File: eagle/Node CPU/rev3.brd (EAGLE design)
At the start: 50 x 50 mm, 44 parts, among them IC1 MEGA8-AI

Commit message: updated to revision 3 of the board
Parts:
- removed PC0, PD0: (no value), pinhead:1X01
- removed PWR: (no value), SparkFun-Passives:1X02
- removed X1: (no value), con-wago-500:W237-102
- added C5: 22pF, resistor:C0603
- added GND_1, PC8, PD8: (no value), pinhead:1X01
- added JP1: (no value), SparkFun-Connectors:SCREWTERMINAL-3.5MM-2
- added VCC_1: VCC, pinhead:1X01
- C1: value 0.1uF -> 22pF
- C2: value 22pF -> 0.1uF
- IC1: value MEGA8-AI -> MEGA88
- MCP1: value (none) -> MCP2515
- MCP2: value MCP2551DIL8 -> MCP2551
- moved PC4 43.1 mm to (32.8, 47.8)
- moved PC7 38.1 mm to (2.29, 17.3)
- moved PC6 38.1 mm to (2.29, 24.9)
- moved PD1 38.1 mm to (48.0, 24.9)
- moved PC3 32.3 mm to (25.1, 47.8)
- moved PD5 31.4 mm to (17.5, 2.03)
- moved PD4 30.5 mm to (9.91, 2.03)
- moved PC5 30.5 mm to (2.29, 40.1)
- moved PD2 27.5 mm to (48.0, 17.3)
- moved PD6 27.5 mm to (25.1, 2.03)
- moved PD7 27.5 mm to (32.8, 2.03)
- moved R5 24.7 mm to (10.6, 24.6), turned to 180 degrees
- moved C1 18.0 mm to (17.8, 38.1), turned to 90 degrees
- moved PC2 17.0 mm to (17.5, 47.8)
- moved PD3 17.0 mm to (48.0, 9.65)
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- renumbered MCP2551 to MCP2
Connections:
- removed net N$36: MCP2.6, X1.2
- new net N$38: MCP1.15, MISO.1, R3.2
- new net N$39: IC1.17, ISP.4, R2.1
- net GND: now also C3.2, C5.1, GND_1.1; no longer C3.1, PWR.2
- net N$1: now also C1.1, IC1.20; no longer IC1.17, MCP1.13, R2.1, SCK.1
- net N$10: now also JP1.1, MCP2.6; no longer C3.2, IC1.7, XTAL.2
- net N$15: now also MCP1.13, R2.2, SCK.1; no longer ISP.2, R4.2
- net N$16: now also JP1.2, MCP2.7; no longer ISP.3, R3.2
- net N$17: now also IC1.15, ISP.2, R4.1; no longer ISP.4, R2.2
- net N$2: now also ISP.3; no longer MCP1.15, MISO.1
- net N$20: now also PC2.1; no longer PC0.1
- net N$22: now also PC5.1; no longer PC2.1
- net N$23: now also PC6.1; no longer PC3.1
- net N$24: now also PC7.1; no longer PC4.1
- net N$25: now also PC8.1; no longer PC5.1
- net N$26: now also PC4.1; no longer PC6.1
- net N$27: now also PC3.1; no longer PC7.1
- net N$28: now also PD4.1; no longer PD0.1
- net N$29: now also PD5.1; no longer PD1.1
- net N$3: now also R4.2; no longer IC1.15, R4.1
- net N$30: now also PD6.1; no longer PD2.1
- net N$31: now also PD7.1; no longer PD3.1
- net N$32: now also PD8.1; no longer PD4.1
- net N$33: now also PD3.1; no longer PD5.1
- net N$34: now also PD2.1; no longer PD6.1
- net N$35: now also PD1.1; no longer PD7.1
- net N$37: now also C4.2, IC1.7, XTAL.1; no longer MCP2.7, X1.1
- net N$9: now also C5.2, XTAL.2; no longer C4.2, XTAL.1
- net VCC: now also C3.1, VCC_1.1; no longer C1.1, PWR.1
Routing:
- net N$38: track 0.00 -> 55.0 mm
- net GND: track 191.6 -> 142.7 mm, vias 0 -> 2
- net N$2: track 54.0 -> 10.9 mm, vias 1 -> 0
- net VCC: track 137.5 -> 98.4 mm
- net N$1: track 47.1 -> 8.18 mm
- net N$15: track 2.96 -> 36.4 mm
- net N$36: track 26.4 -> 0.00 mm
- net N$16: track 2.96 -> 24.3 mm
- net N$37: track 25.3 -> 13.6 mm
- net N$7: track 31.8 -> 22.0 mm
- net N$39: track 0.00 -> 8.99 mm
- net N$17: track 2.96 -> 11.9 mm
- net N$10: track 16.2 -> 24.5 mm
- net N$5: track 32.5 -> 24.5 mm
- net N$14: track 22.4 -> 16.0 mm
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- added copper zone on layer 1, net GND
- added copper zone on layer 16, net GND
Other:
- board text added: "HI"
- board text added: "LO"
- board text added: "Node CPU Rev. 3"
- board text added: "Rev 3"
- board text removed: "Node CPU Rev. 1"
- board text removed: "Revision 1"

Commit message: update rev3 schematic
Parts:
- XTAL: device special:QS -> crystal:HC49/S
- moved C3 3.63 mm to (20.6, 18.8), turned to 180 degrees
- moved C2 1.17 mm to (20.6, 21.0), turned to 180 degrees
- moved C4 0.25 mm to (23.1, 10.7)
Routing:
- net GND: track 142.7 -> 139.0 mm
- net N$31: track 35.9 -> 36.9 mm
- net N$30: track 31.1 -> 32.1 mm
- net N$32: track 41.8 -> 42.7 mm
- net N$9: track 13.7 -> 14.2 mm

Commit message: update rev3 board schematic
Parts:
- removed PC6, PC7, PC8, PD8: (no value), pinhead:1X01
- added ADC6, ADC7, PC0, PD0: (no value), pinhead:1X01
- added C6, C7: 0.1uF, resistor:C0603
- moved PC4 43.1 mm to (2.29, 17.3)
- moved PD1 38.1 mm to (17.5, 2.03)
- moved PC3 32.3 mm to (2.29, 24.9)
- moved PD5 31.4 mm to (48.0, 9.65)
- moved PD4 30.5 mm to (40.4, 2.03)
- moved PC5 30.5 mm to (2.29, 9.65)
- moved PD2 27.5 mm to (25.1, 2.03)
- moved PD6 27.5 mm to (48.0, 17.3)
- moved PD7 27.5 mm to (48.0, 24.9)
- moved PC2 17.0 mm to (2.29, 40.1)
- moved PD3 17.0 mm to (32.8, 2.03)
- moved R6 1.02 mm to (31.9, 23.1)
- moved MCP1 0.77 mm to (38.4, 32.4)
- moved RX 0.76 mm to (39.9, 19.1)
- moved TX 0.76 mm to (39.9, 16.8)
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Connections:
- net GND: now also C6.2, C7.2
- net N$20: now also PC0.1; no longer PC2.1
- net N$22: now also PC2.1; no longer PC5.1
- net N$23: now also PC3.1; no longer PC6.1
- net N$24: now also PC4.1; no longer PC7.1
- net N$25: now also PC5.1; no longer PC8.1
- net N$26: now also ADC6.1; no longer PC4.1
- net N$27: now also ADC7.1; no longer PC3.1
- net N$28: now also PD0.1; no longer PD4.1
- net N$29: now also PD1.1; no longer PD5.1
- net N$30: now also PD2.1; no longer PD6.1
- net N$31: now also PD3.1; no longer PD7.1
- net N$32: now also PD4.1; no longer PD8.1
- net N$33: now also PD5.1; no longer PD3.1
- net N$34: now also PD6.1; no longer PD2.1
- net N$35: now also PD7.1; no longer PD1.1
- net VCC: now also C6.1, C7.1
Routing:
- net GND: track 139.0 -> 74.9 mm, vias 2 -> 3
- net N$7: track 22.0 -> 29.3 mm
- net N$14: track 16.0 -> 20.2 mm
- net RXLED: track 21.7 -> 20.2 mm
- net VCC: track 98.9 -> 97.9 mm, vias 2 -> 1
- net N$3: track 43.2 -> 42.4 mm
- net N$38: track 55.0 -> 55.8 mm
- net N$15: track 36.4 -> 37.2 mm
- net N$4: track 11.4 -> 10.7 mm
- net N$5: track 24.5 -> 23.9 mm
- net N$16: track 24.3 -> 23.7 mm
- net N$10: track 24.5 -> 23.9 mm
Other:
- board text added: "RST"
- board text added: "RX"
- board text added: "SCL"
- board text added: "SDA"
- board text added: "TX"

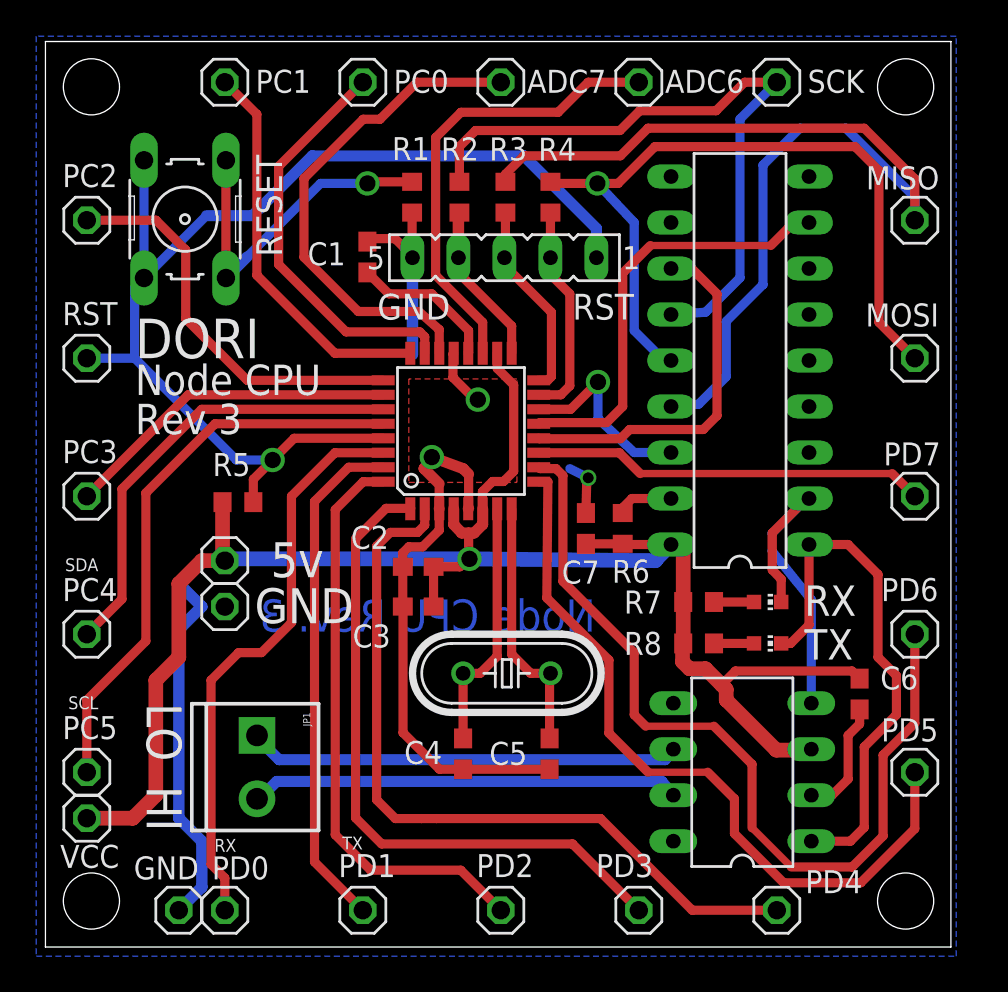
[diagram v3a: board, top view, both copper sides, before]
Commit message: add power LED to node cpu board
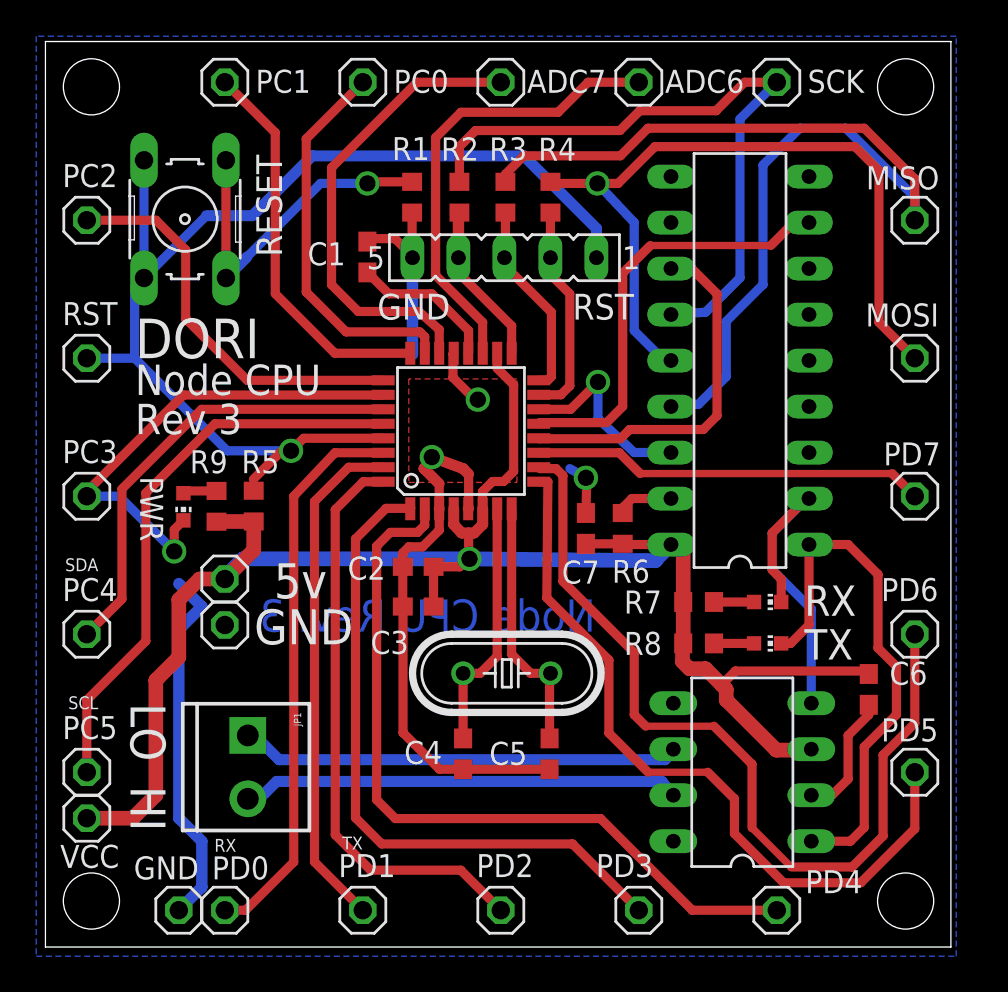
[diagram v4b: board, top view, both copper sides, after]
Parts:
- added PWR: (no value), led:CHIP-LED0603
- added R9: 470, resistor:R0603
- moved GND_1 1.02 mm to (9.91, 17.8)
- moved VCC_1 1.02 mm to (9.91, 20.3)
- moved R5 0.90 mm to (11.5, 24.3), turned to 270 degrees
- moved C6 0.57 mm to (45.5, 14.2)
- moved JP1 0.51 mm to (11.2, 11.7)
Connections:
- removed net N$23: IC1.26, PC3.1
- new net N$36: PWR.A, R9.1
- new net N$40: IC1.26, PC3.1, PWR.C
- net VCC: now also R9.2
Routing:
- net N$40: track 0.00 -> 26.8 mm, vias 0 -> 1
- net N$23: track 18.7 -> 0.00 mm
- net VCC: track 97.9 -> 100.5 mm
- net N$36: track 0.00 -> 1.88 mm
- net N$27: track 27.8 -> 26.0 mm
- net N$20: track 22.6 -> 21.4 mm
- net N$28: track 31.8 -> 31.1 mm
- net N$16: track 23.7 -> 24.2 mm

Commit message: nodes have custom hardware bases now
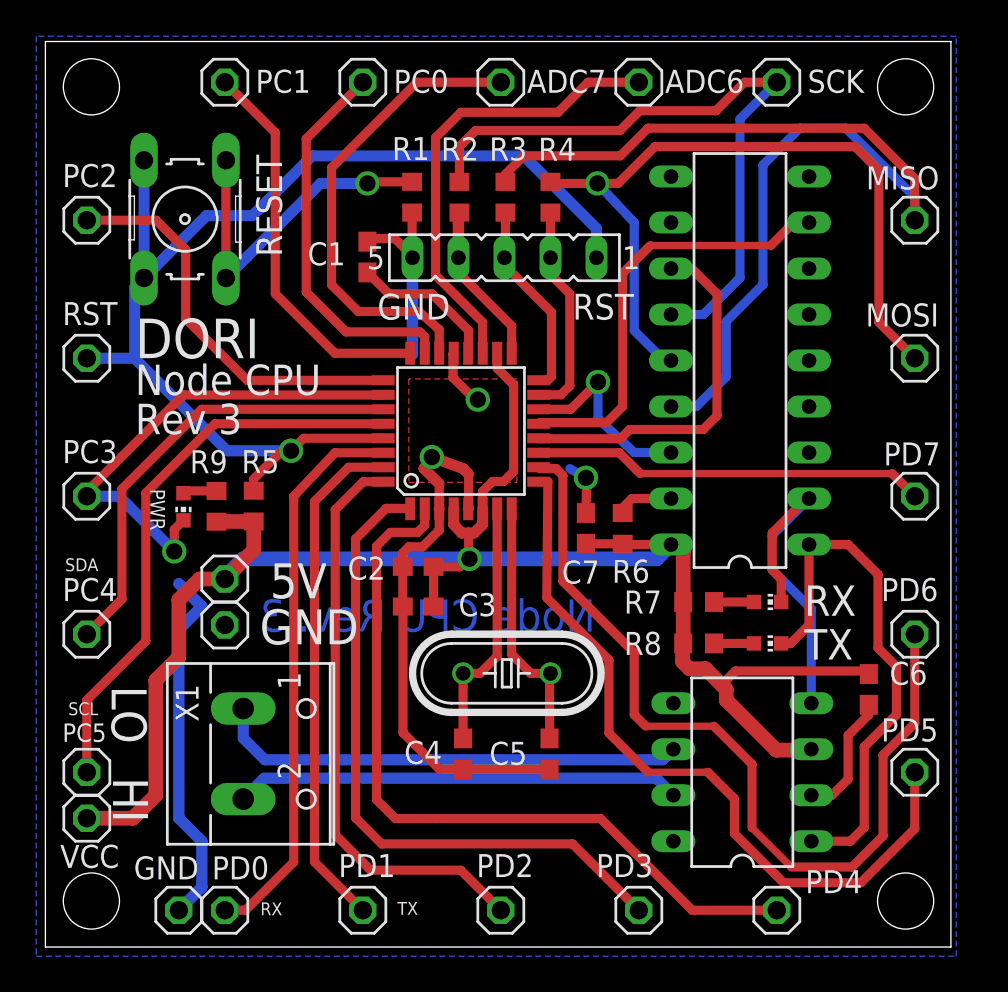
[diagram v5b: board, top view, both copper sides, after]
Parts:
- removed JP1: (no value), SparkFun-Connectors:SCREWTERMINAL-3.5MM-2
- added X1: (no value), con-wago-500:W237-102
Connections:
- net N$10: now also X1.1; no longer JP1.1
- net N$16: now also X1.2; no longer JP1.2
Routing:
- net N$10: track 24.3 -> 26.1 mm
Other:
- board text added: "5V"
- board text removed: "5v"
